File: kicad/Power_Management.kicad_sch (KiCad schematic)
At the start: 10 parts, among them U4 ADP150AUJZ-3.3-R7

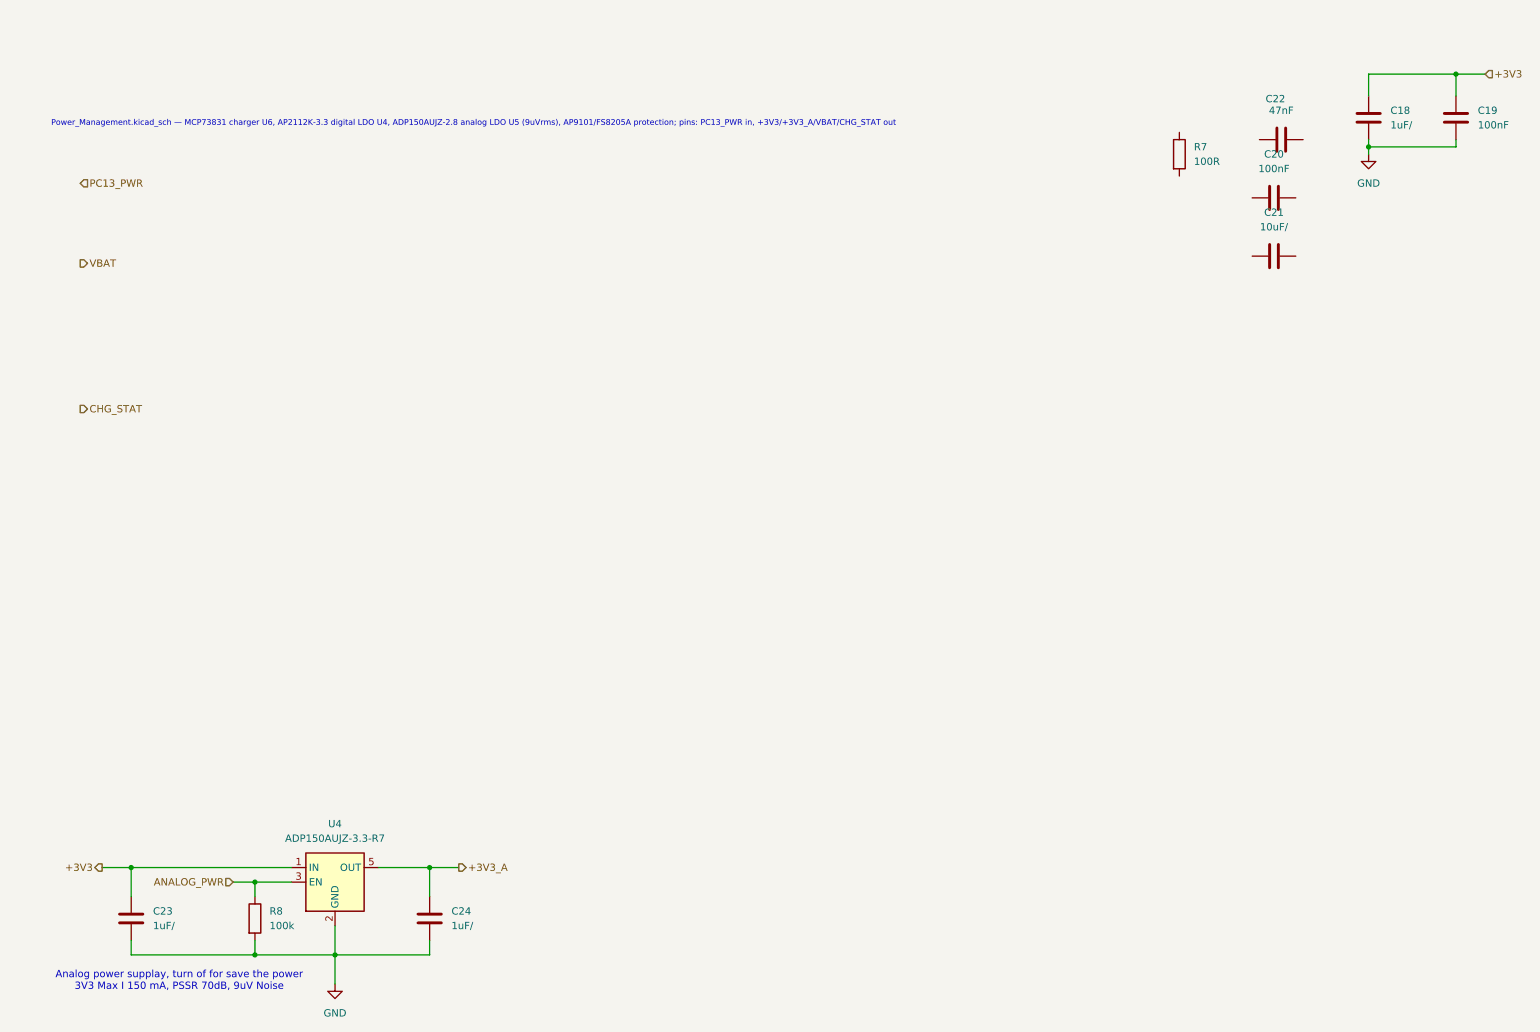
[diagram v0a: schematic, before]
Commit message: Add calibration scripts, documentation, simulation tools, and KiCad updates
- cal/calibration.py: 3-phase RF linearity calibration (29 freq, 28 power steps,
  1 MHz–10 GHz, direct generator→DUT, no attenuator, NRP sensor 0.01 dBm precision)
- cal/temp_calibration.py: temperature calibration via Vötsch chamber (16–40°C,
  Vötsch SIMSERV TCP driver, tracking generator source, outputs TEMP_COEFF_DB_PER_C[])
- cal/results/: dry-run calibration tables (.h/.json), figures, PDF reports
- doc/: ADC signal path analysis, calibration procedure (3-phase), lab optimisation
  guide updated for 1 MHz–10 GHz range and temperature correction firmware formula
- doc/diagrams/: PlantUML/Mermaid source + rendered PNGs for pipeline, firmware,
  and RF signal chain architectures
- sim/ltpwr_to_touchstone.py: LTpowerAnalyzer Z(f) → Touchstone S1P + Z1P via
  scikit-rf for SIwave PI-AC Decoupling Optimization DC/DC source impedance import
- sim/Measured_source_impedance.txt/.s1p/.z1p: DC/DC output impedance measurement
  and converted Touchstone files (100 Hz–10 MHz, 201 points)
- kicad/: updated schematics (MCU, power management, RF frontend, UI) and PCB layout
- kicad/fixture-rev_A/: test fixture DXF drawings
- lib/: Würth 744231091 datasheet, Hammond 1590A board outline footprint
- pp_3d_printer_setup_spec.md, pp_horn_antenna_manufacturing_spec.md: process specs

Co-Authored-By: Claude Sonnet 4.6 <noreply@anthropic.com>
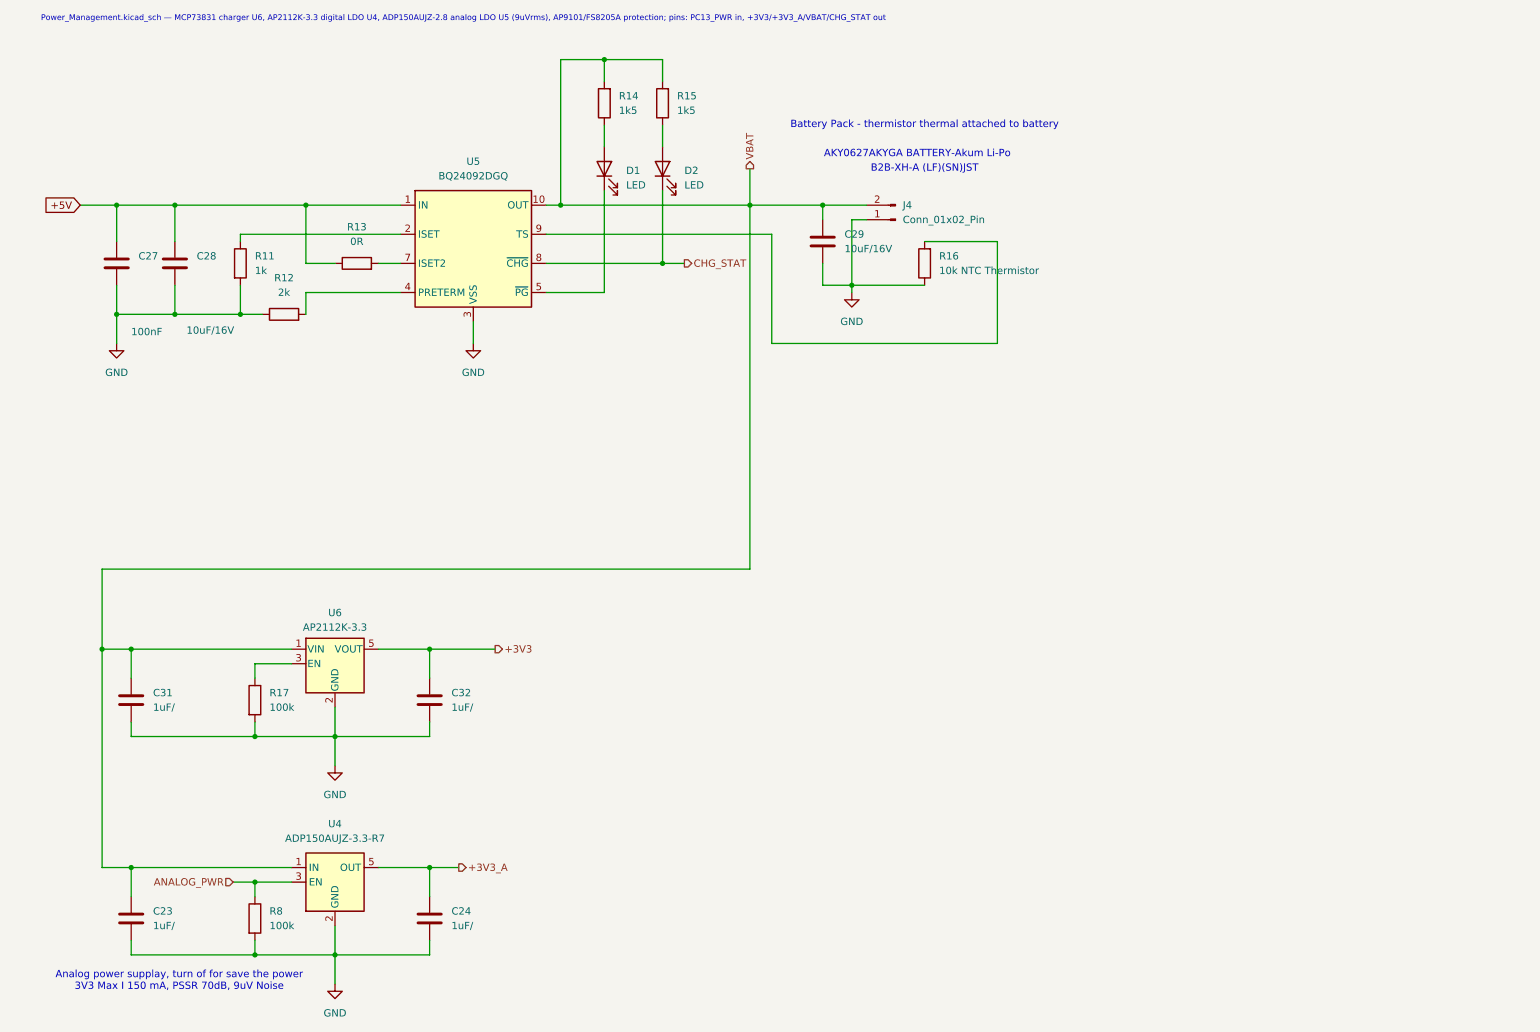
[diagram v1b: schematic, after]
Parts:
- removed C18: 1uF/, Capacitor_SMD:C_0201_0603Metric, symbol Device:C
- removed C19, C20: 100nF, Capacitor_SMD:C_0402_1005Metric, symbol Device:C
- removed C21: 10uF/, Capacitor_SMD:C_0201_0603Metric, symbol Device:C
- removed C22: 47nF, Capacitor_SMD:C_0402_1005Metric, symbol Device:C
- removed R7: 100R, Resistor_SMD:R_0402_1005Metric, symbol Device:R
- added C27: 100nF, Capacitor_SMD:C_0402_1005Metric, symbol Device:C
- added C28, C29: 10uF/16V, Capacitor_SMD:C_0402_1005Metric, symbol Device:C
- added C31, C32: 1uF/, Capacitor_SMD:C_0201_0603Metric, symbol Device:C
- added D1, D2: LED, LED_SMD:LED_0402_1005Metric, symbol Device:LED
- added J4: Conn_01x02_Pin, Connector_JST:JST_XH_B2B-XH-AM_1x02_P2.50mm_Vertical, symbol Connector:Conn_01x02_Pin
- added R11: 1k, Resistor_SMD:R_0402_1005Metric, symbol Device:R
- added R12: 2k, Resistor_SMD:R_0402_1005Metric, symbol Device:R
- added R13: 0R, Resistor_SMD:R_0402_1005Metric, symbol Device:R
- added R14, R15: 1k5, Resistor_SMD:R_0402_1005Metric, symbol Device:R
- added R16: 10k NTC Thermistor, Capacitor_SMD:C_0201_0603Metric, symbol Device:R
- added R17: 100k, Resistor_SMD:R_0402_1005Metric, symbol Device:R
- added U5: BQ24092DGQ, Package_SO:HVSSOP-10-1EP_3x3mm_P0.5mm_EP1.83x1.89mm_ThermalVias, symbol Battery_Management:BQ24090DGQ
- added U6: AP2112K-3.3, Package_TO_SOT_SMD:SOT-23-5, symbol Regulator_Linear:AP2112K-3.3
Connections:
- net +3V3: now also C32.2, U6.5 (VOUT); no longer C23.2, U4.1 (IN)
- net CHG_STAT: now also D2.1 (K), U5.8 (~{CHG})
- net GND: now also C27.2, C28.2, C29.2, C31.1, C32.1, J4.1 (Pin_1), R11.2, R12.1, R16.1, R17.2, U5.11 (VSS), U5.3 (VSS), U6.2 (GND)
- net VBAT: now also C23.2, U4.1 (IN), C29.1, C31.2, J4.2 (Pin_2), R14.2, R15.2, U5.10 (OUT), U6.1 (VIN)
- new net: R16.2, U5.9 (TS)
- new net: D2.2 (A), R15.1
- new net: R12.2, U5.4 (PRETERM)
- new net: R17.1, U6.3 (EN)
- new net: R11.1, U5.2 (ISET)
- new net: D1.1 (K), U5.5 (~{PG})
- new net: R13.2, U5.7 (ISET2)
- new net: D1.2 (A), R14.1
- new net +5V: C27.1, C28.1, R13.1, U5.1 (IN)
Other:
- note added: "AKY0627AKYGA BATTERY-Akum Li-Po"
- note added: "B2B-XH-A (LF)(SN)JST"
- note added: "Battery Pack - thermistor thermal attached to battery"
- title: Power Management -> RF Frontend
